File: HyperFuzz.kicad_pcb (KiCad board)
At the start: 2 copper layers, 56 x 54 mm, 62 parts, among them J1 9V, J2 G, J3 IN/LED/GND/OUT, J4 IG, J5 OG, U1 TL072, U2 TL072, U3 TL072

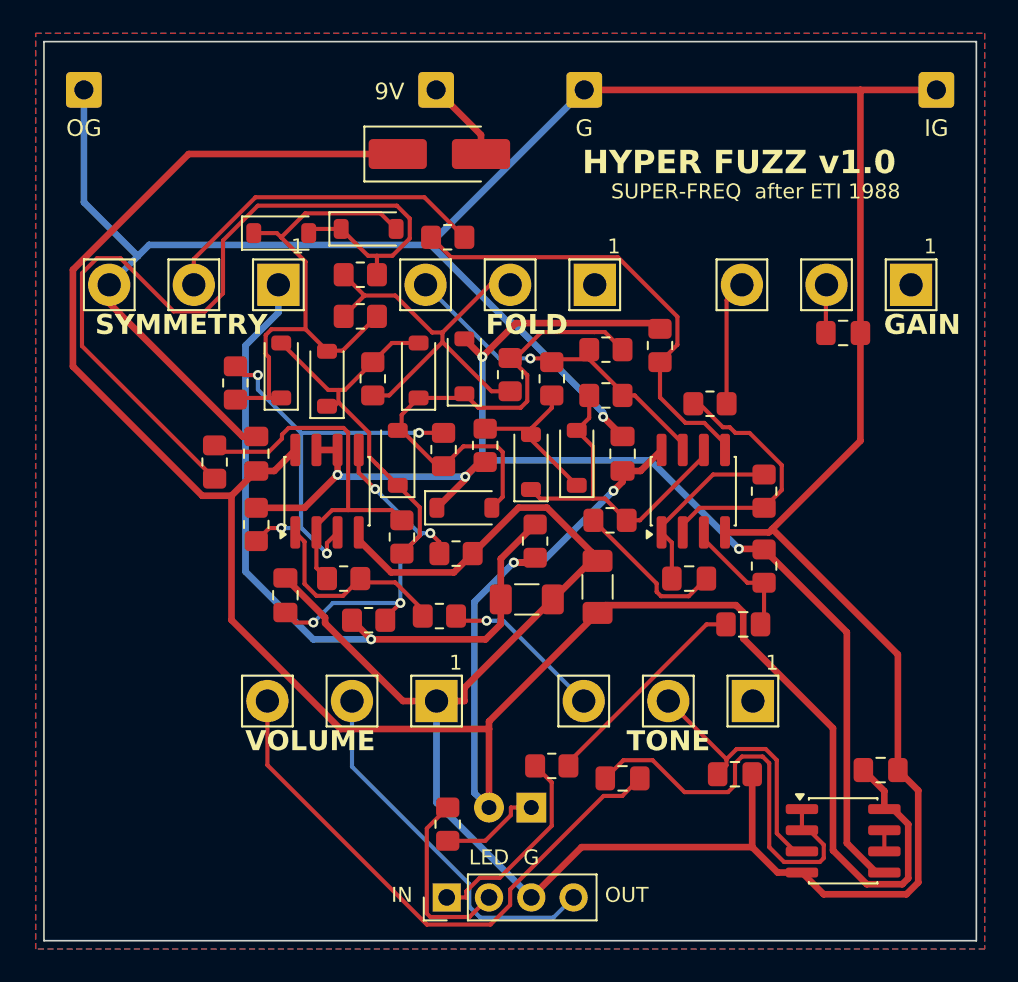
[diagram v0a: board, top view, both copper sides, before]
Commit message: Hyper Fuzz v1.1: 9 mm pots, new knob grid, wire pads moved, enclosure drilling
As ordered from JLCPCB (October 2026 batch).

Co-Authored-By: Claude Opus 5.5 <noreply@anthropic.com>
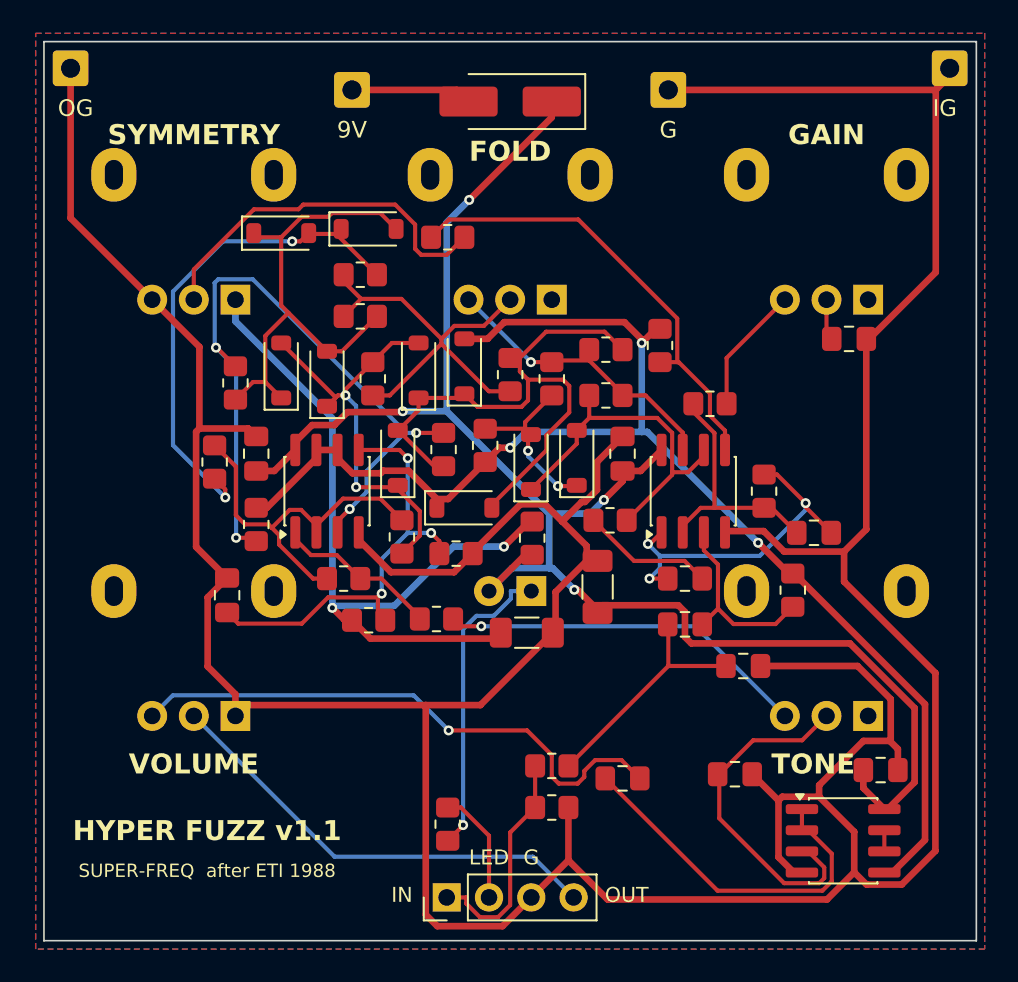
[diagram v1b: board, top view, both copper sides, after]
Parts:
- added C12: 1n, Capacitor_SMD:C_0805_2012Metric_Pad1.18x1.45mm_HandSolder, F.Cu at (164.0, 137.5)
- added C13: 100p, Capacitor_SMD:C_0805_2012Metric_Pad1.18x1.45mm_HandSolder, F.Cu at (168.2, 129.5)
- added R27: 1M, Resistor_SMD:R_0805_2012Metric_Pad1.20x1.40mm_HandSolder, F.Cu at (152.5, 146.0)
- RV1, RV2, RV3, RV4, RV5: footprint UglyFace:Potentiometer_Alpha_16mm_Vertical -> Potentiometer_THT:Potentiometer_Alpha_RD901F-40-00D_Single_Vertical; moved to B.Cu
- U3: value TL072 -> LM358
- moved D12 13.0 mm to (151.3, 133.0)
- moved RV4 12.0 mm to (171.5, 140.5), turned to 90 degrees
- moved RV5 7.06 mm to (133.5, 140.5), turned to 90 degrees
- moved D11 5.29 mm to (150.0, 103.6), turned to 180 degrees
- moved J1 5.05 mm to (140.5, 102.9)
- moved J2 5.05 mm to (159.5, 102.9)
- moved C1 3.50 mm to (160.5, 135.0)
- moved C8 3.50 mm to (133.0, 133.2)
- moved RV1 2.66 mm to (171.5, 115.5), turned to 90 degrees
- moved RV2 2.66 mm to (152.5, 115.5), turned to 90 degrees
- moved RV3 2.66 mm to (133.5, 115.5), turned to 90 degrees
- moved R2 2.25 mm to (167.0, 132.9)
- moved C7 2.00 mm to (151.0, 135.5)
- moved J4 1.53 mm to (176.4, 101.6)
- moved J5 1.53 mm to (123.6, 101.6)
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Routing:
- net +9V: track 154.5 -> 99.3 mm, vias 2 -> 4
- net Net-(D3-K): track 51.4 -> 30.2 mm, vias 0 -> 2
- net GND: track 240.9 -> 261.2 mm, vias 1 -> 0
- net /SUM_P: track 27.1 -> 44.1 mm
- net Net-(R22-Pad2): track 9.78 -> 22.3 mm
- net Net-(D12-K): track 6.12 -> 18.4 mm, vias 0 -> 1
- net /PRE: track 10.9 -> 20.8 mm, vias 0 -> 3
- net Net-(U3A-+): track 16.0 -> 21.1 mm
- net /OUT: track 22.3 -> 27.3 mm
- net /LED_K: track 11.2 -> 6.89 mm
- net Net-(U2B-+): track 22.4 -> 26.6 mm, vias 4 -> 3
- net Net-(D10-A): track 31.7 -> 35.7 mm
- net Net-(U1A-+): track 7.70 -> 11.6 mm
- net Net-(U3A--): track 25.4 -> 21.9 mm
- net /DRIVE: track 20.6 -> 18.0 mm
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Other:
- board text added: "HYPER FUZZ v1.1"
- board text removed: "HYPER FUZZ v1.0"
